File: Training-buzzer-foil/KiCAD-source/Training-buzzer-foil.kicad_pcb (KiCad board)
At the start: 2 copper layers, 13 parts, among them J1 Con, J2 DC Jack, Q1 BC547B, Q2 BC547B, Q3 BC547B

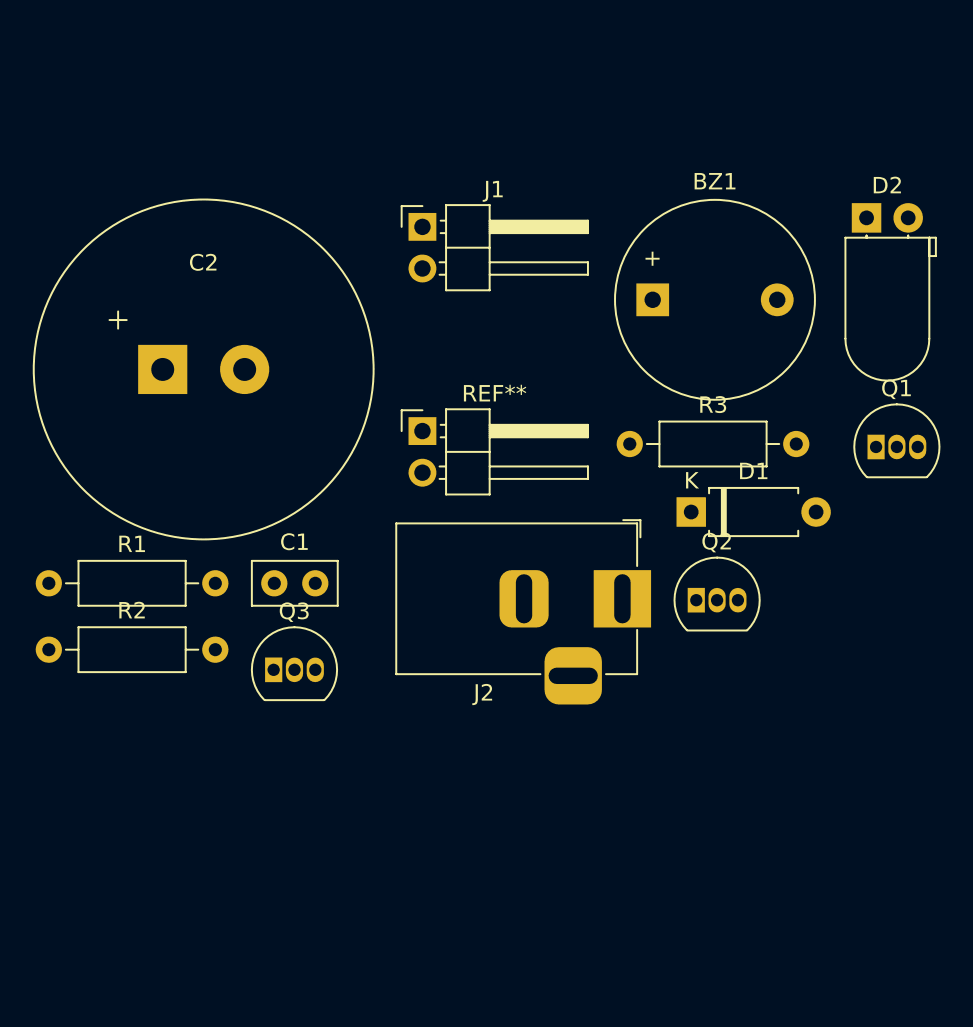
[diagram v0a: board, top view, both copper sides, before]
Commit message: Create PCB for foil training buzzer
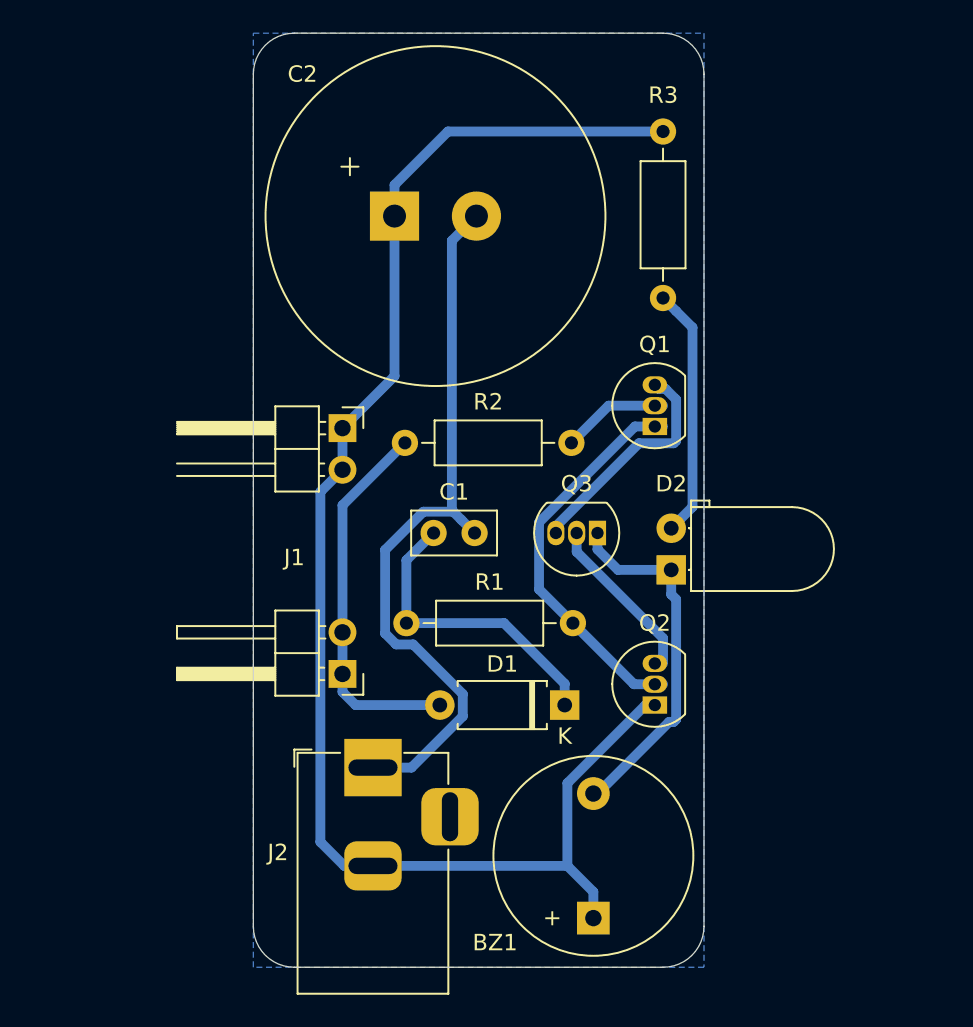
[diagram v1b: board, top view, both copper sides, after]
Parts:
- moved BZ1 37.9 mm to (157.8, 126.0), turned to 90 degrees
- moved R2 34.3 mm to (156.4, 97.0), turned to 180 degrees
- moved R1 32.1 mm to (156.5, 108.0), turned to 180 degrees
- moved J1 27.7 mm to (142.4, 111.1), turned to 180 degrees
- moved D2 24.6 mm to (162.5, 104.8), turned to 90 degrees
- moved Q3 21.5 mm to (158.0, 102.5), turned to 180 degrees
- moved R3 19.2 mm to (162.0, 78.0), turned to 270 degrees
- moved J2 18.4 mm to (144.3, 116.8), turned to 90 degrees
- moved C2 17.0 mm to (145.6, 83.2)
- moved D1 14.1 mm to (156.0, 113.0), turned to 180 degrees
- moved Q1 13.6 mm to (161.5, 96.0), turned to 90 degrees
- moved C1 10.2 mm to (148.0, 102.5)
- moved Q2 6.88 mm to (161.5, 113.0), turned to 90 degrees
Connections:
- Q1 pad 2: Net-(Q1-Pad1) -> Net-(Q1-Pad2)
- R2 pad 1: Net-(Q1-Pad1) -> Net-(Q1-Pad2)
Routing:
- net Net-(BZ1-Pad1): track 0.00 -> 91.6 mm
- net Net-(C1-Pad2): track 0.00 -> 59.6 mm
- net Net-(Q1-Pad1): track 0.00 -> 24.0 mm
- net Net-(D1-Pad2): track 0.00 -> 23.0 mm
- net Net-(BZ1-Pad2): track 0.00 -> 21.9 mm
- net Net-(C1-Pad1): track 0.00 -> 18.7 mm
- net Net-(D2-Pad2): track 0.00 -> 15.3 mm
- net Net-(Q2-Pad3): track 0.00 -> 10.1 mm
- net Net-(Q1-Pad2): track 0.00 -> 6.53 mm
- added copper zone on B.Cu, net Net-(C1-Pad2)
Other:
- board outline added: 27.5 x 57 mm
